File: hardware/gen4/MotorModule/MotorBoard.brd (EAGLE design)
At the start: 30.5 x 66.5 mm, 64 parts, among them IC1 XMEGA16A4A, M1O1 TEST_PT, M1O2 TEST_PT, M1O3 TEST_PT

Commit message: Motor board done (pending review)
layout + schematic done (got it down to 3x5 cm, couldn't go much smaller
unless I used smaller than 0806)
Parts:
- removed C14, C15, C3: 0.1uF, SparkFun-Passives:0805
- removed JP2: M20X2SHROUDED, SparkFun-Connectors:2X20_SHROUDED
- removed S1: SWITCH-MOMENTARY-2SMD-4, SparkFun-Electromechanical:TACTILE_SWITCH_TALL
- added JP3: M20X2SHROUDED_SMT, SparkFun-Connectors:2X20_SHROUDED_SMT
- added JP4: (no value), SparkFun-Connectors:1X04_SMD_RA_FEMALE
- added R16, R17: 2K, SparkFun-Resistors:0805
- added S2: TAC_SWITCHSMD, SparkFun-Retired:TACTILE-SWITCH-SMD
- added U$2: MOTORCON, gen3:GEN3CON
- moved IC2 198.0 mm to (26.2, 12.0), flipped to the bottom
- moved JP1 195.0 mm to (25.0, -4.00), turned to 180 degrees
- moved R11 182.3 mm to (21.0, 7.00)
- moved R5 182.1 mm to (28.0, 25.5), turned to 270 degrees
- moved R15 177.7 mm to (14.2, -12.0)
- moved R7 169.8 mm to (15.4, 6.24), turned to 90 degrees
- moved R9 169.3 mm to (11.5, 6.24), turned to 90 degrees
- moved C13 161.3 mm to (20.6, 8.60)
- moved C12 158.6 mm to (21.0, 11.0), turned to 180 degrees
- moved C1 155.8 mm to (21.0, 14.5), turned to 180 degrees
- moved U$1 134.2 mm to (15.0, 13.0)
- moved IC1 119.0 mm to (13.5, -4.50)
- moved GEN_4_REV_A 86.6 mm to (0.00, 55.2)
- moved FRAME7 53.5 mm to (-68.9, 53.5), flipped to the top
- moved R78 37.1 mm to (18.8, -12.5)
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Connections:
- removed net 5V: R105.2, R106.2, R107.2
- removed net N$25: C3.2, U$1.5
- removed net N$26: C14.1, U$1.4
- removed net N$27: C14.2, U$1.3
- removed net N$29: C15.1, U$1.2
- removed net N$30: C15.2, U$1.1
- net 12V: now also JP3.1, JP3.2, JP3.3, JP3.4; no longer JP2.1, JP2.2, JP2.3, JP2.4, JP2.5, JP2.6
- net 12VGND: now also JP3.37, JP3.38, JP3.39, JP3.40, R5.2; no longer JP2.35, JP2.36, JP2.37, JP2.38, JP2.39, JP2.40
- net 3.3V: now also C12.2, JP4.1, R105.2, R106.2, R107.2, R17.2, U$1.24, U$2.1, U$5.1
- net GND: now also JP4.3, R16.1, S2.4, U$1.P$1, U$2.5; no longer S1.B2, U$1.41-1, U$1.41-10, U$1.41-11, U$1.41-12, U$1.41-13, U$1.41-14, U$1.41-15, U$1.41-16, U$1.41-2, U$1.41-3, U$1.41-4, U$1.41-5, U$1.41-6, U$1.41-7, U$1.41-8, U$1.41-9
- net M1H1: now also U$1.5, U$2.3; no longer JP2.19
- net M1H2: now also U$1.3, U$2.4; no longer JP2.17
- net M1H3: now also U$1.1, U$2.2; no longer JP2.21
- net M1O1: now also U$2.10, U$2.11; no longer JP2.7, JP2.8
- net M1O2: now also U$2.8, U$2.9; no longer JP2.10, JP2.9
- net M1O3: now also U$2.6, U$2.7; no longer JP2.11, JP2.12
- net M1QA: now also JP4.2; no longer JP2.23
- net M1QB: now also JP4.4; no longer JP2.25
- net N$2: now also U$1.29; no longer U$1.30
- net N$22: now also R16.2, R17.1, U$1.2, U$1.4; no longer C3.1
- net N$3: now also JP3.31; no longer JP2.29
- net N$33: now also JP3.34, JP3.36; no longer JP2.32, JP2.34
- net N$34: now also JP3.35; no longer JP2.33
- net N$4: now also JP3.33; no longer JP2.31
- net N$45: now also JP3.29; no longer JP2.27
- net N$5: no longer R5.2
- net N$9: now also U$1.30; no longer U$1.29
- net RESET: now also S2.2; no longer S1.A2
- net VREG: no longer C12.2, U$1.24, U$5.1
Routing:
- net GND: track 0.00 -> 181.2 mm, vias 0 -> 9
- net 3.3V: track 0.00 -> 117.8 mm, vias 0 -> 8
- net 12V: track 0.00 -> 113.7 mm, vias 0 -> 5
- net 12VGND: track 0.00 -> 81.4 mm, vias 0 -> 3
- net TSENSE1: track 0.00 -> 61.8 mm, vias 0 -> 1
- net M1O1: track 0.00 -> 57.2 mm, vias 0 -> 2
- net M1O3: track 0.00 -> 54.0 mm, vias 0 -> 1
- net N$17: track 0.00 -> 49.1 mm, vias 0 -> 2
- net N$98: track 0.00 -> 46.9 mm
- net M1H1: track 0.00 -> 45.7 mm, vias 0 -> 3
- net RESET: track 0.00 -> 42.9 mm, vias 0 -> 3
- net M1O2: track 0.00 -> 40.2 mm, vias 0 -> 3
- net N$21: track 0.00 -> 39.1 mm, vias 0 -> 2
- net BREN: track 0.00 -> 37.9 mm, vias 0 -> 2
- net N$18: track 0.00 -> 37.8 mm
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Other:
- board size 30.5 x 66.5 mm -> 30.2 x 58.8 mm
- board text removed: "Pin1"

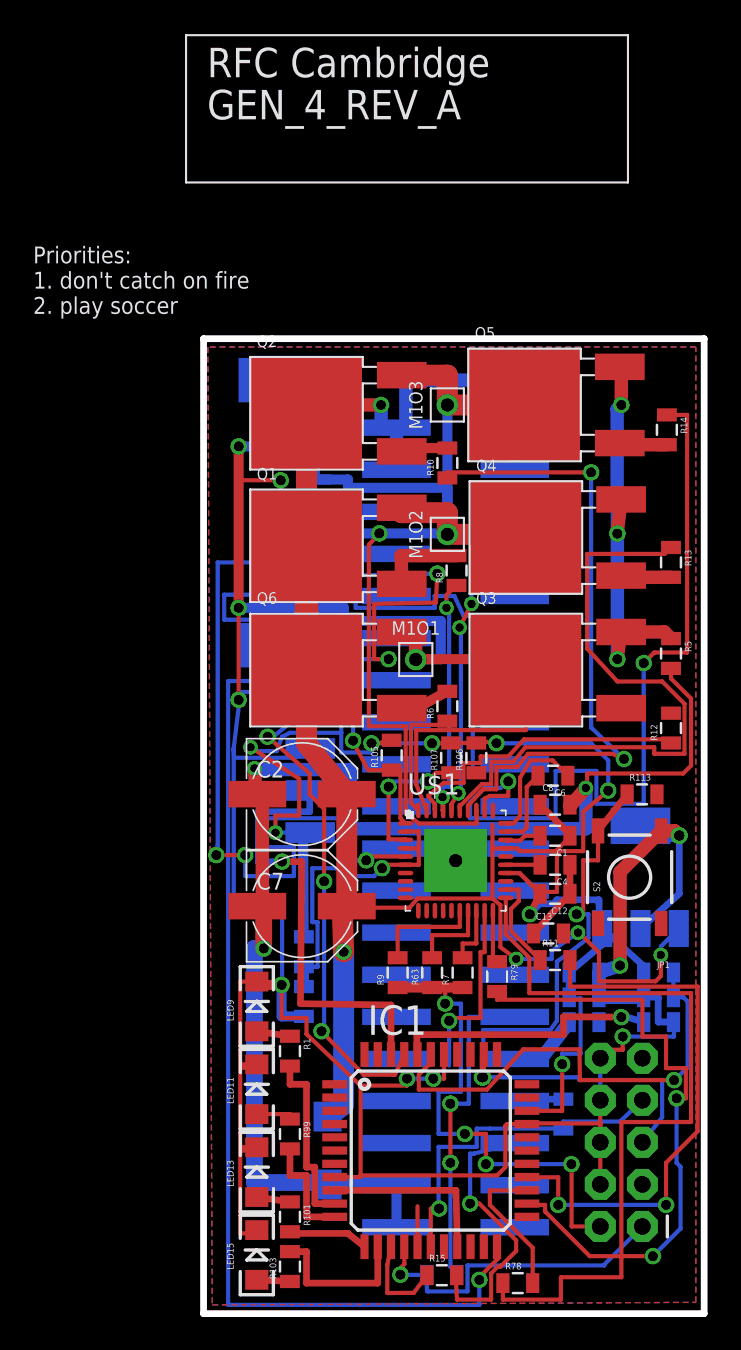
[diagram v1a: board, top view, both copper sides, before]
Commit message: Few overlap edits
Also need to fix qfn package part,  the part needs a smt pad added.
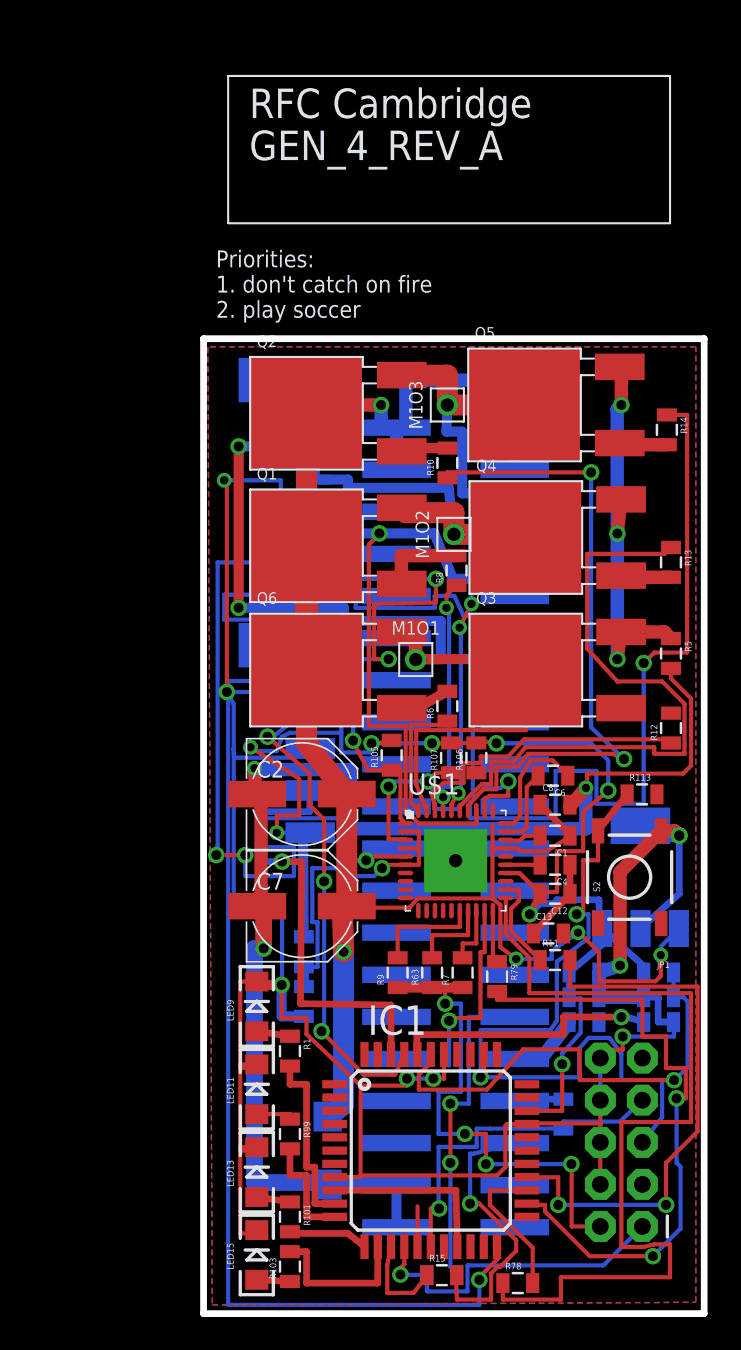
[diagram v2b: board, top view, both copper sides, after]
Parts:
- moved GEN_4_REV_A 3.54 mm to (2.54, 52.7)
- moved M1O2 0.40 mm to (14.9, 32.7)
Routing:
- net M1O3: track 54.0 -> 72.4 mm
- net M1H2: track 32.7 -> 46.4 mm
- net N$98: track 46.9 -> 53.0 mm
- net RESET: track 42.9 -> 45.9 mm, vias 3 -> 2
- net GND: track 181.2 -> 182.6 mm
- net 3.3V: track 117.8 -> 116.9 mm

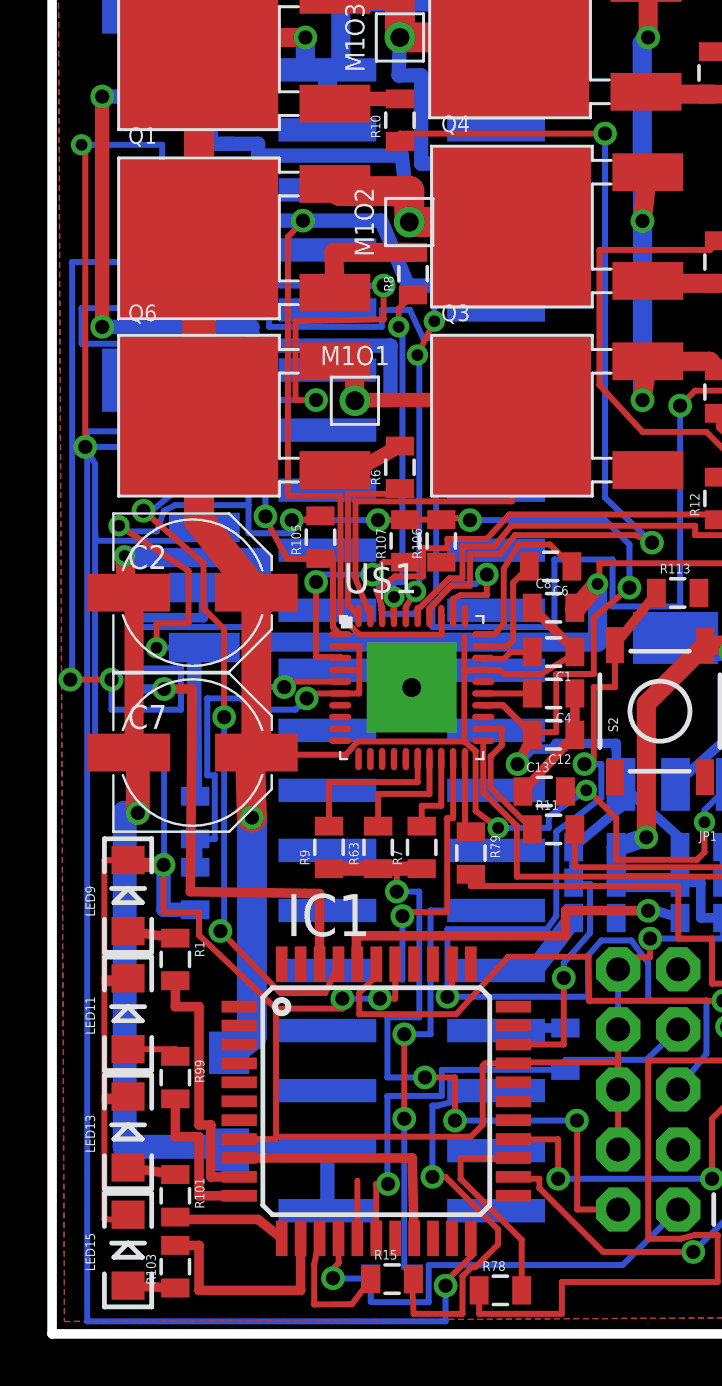
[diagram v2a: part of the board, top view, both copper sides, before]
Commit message: Slight fixes
fixed qfn package and overlap
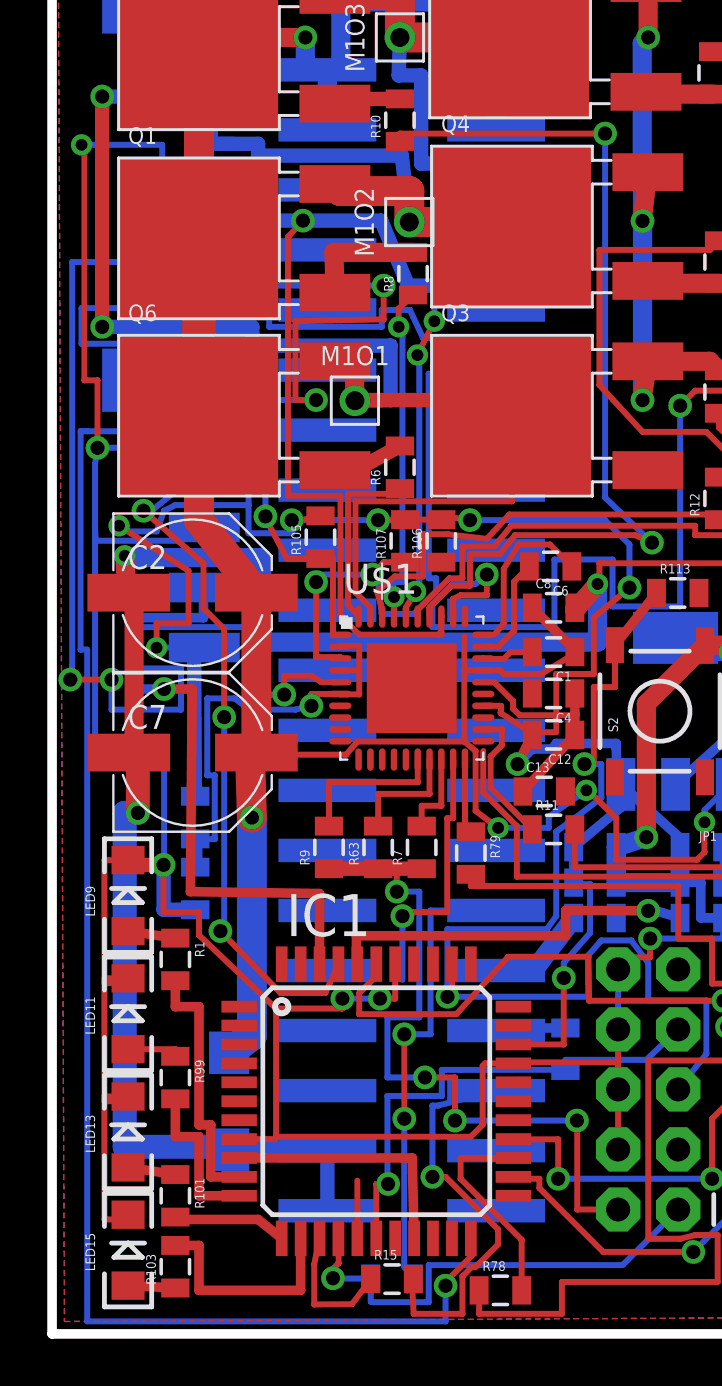
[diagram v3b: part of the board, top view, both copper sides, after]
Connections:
- net GND: now also U$1.P$3; no longer U$1.P$1
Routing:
- net GND: track 182.6 -> 187.2 mm
- net 3.3V: track 116.9 -> 114.5 mm
- net N$15: track 2.08 -> 0.00 mm
- net M1H1: track 45.8 -> 47.0 mm
- net M1H2: track 46.4 -> 47.1 mm
- net TSENSE1: track 61.8 -> 62.4 mm

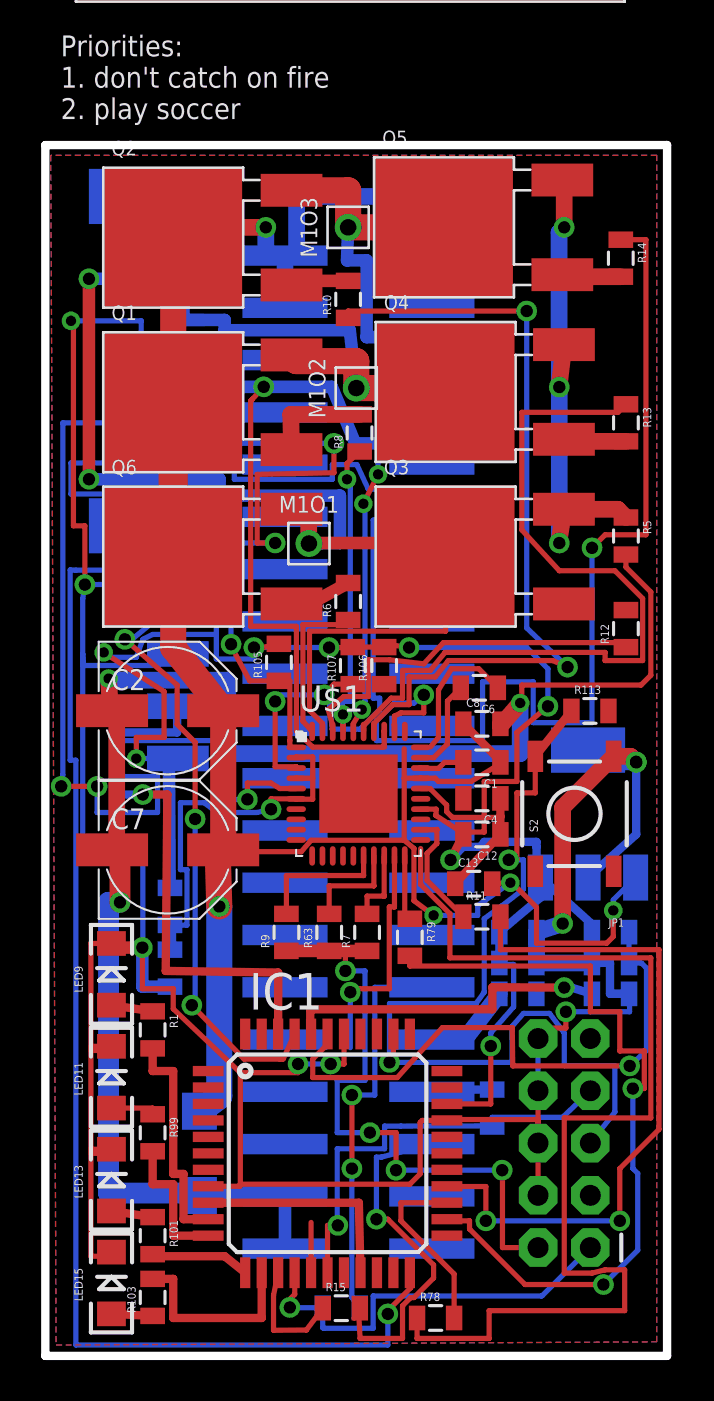
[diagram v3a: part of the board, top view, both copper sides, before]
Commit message: fixed overlaps, nearly finished routing
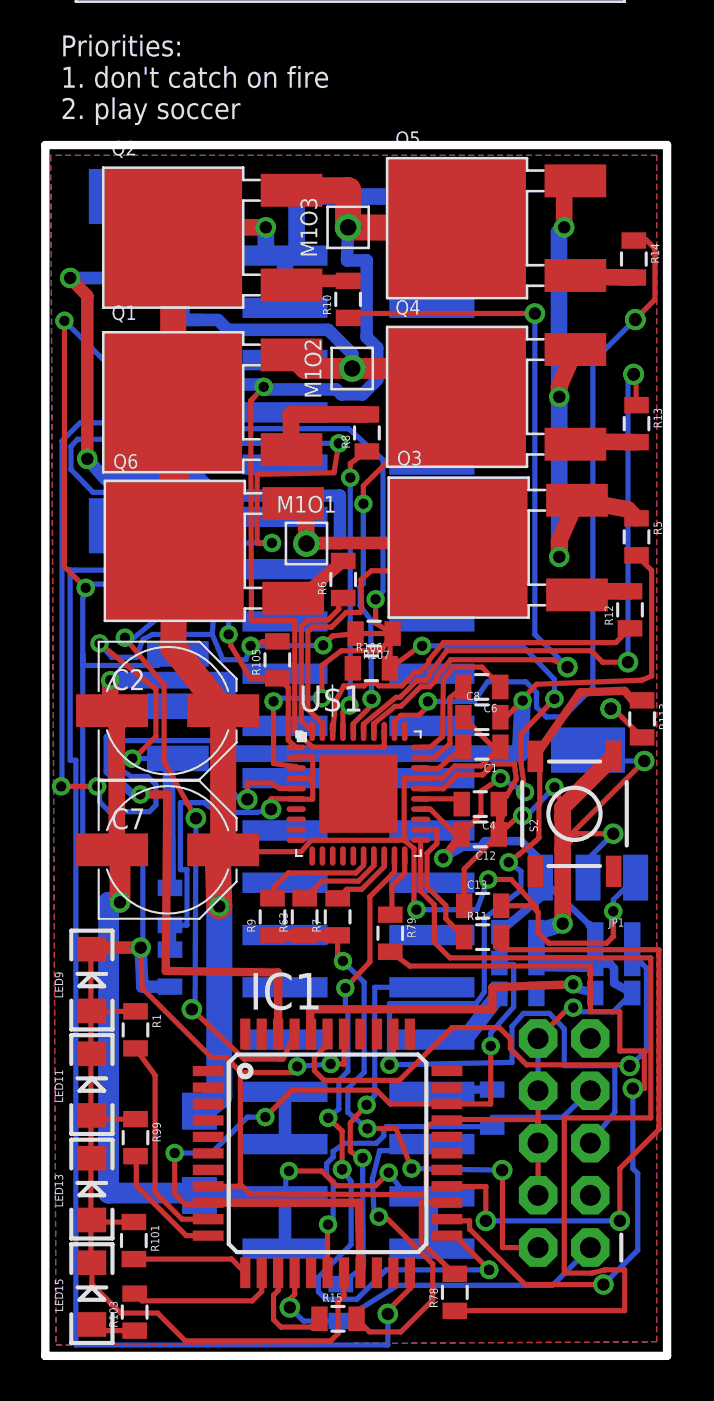
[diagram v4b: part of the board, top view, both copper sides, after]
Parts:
- moved R113 2.57 mm to (28.8, 16.6), turned to 270 degrees
- moved R107 1.87 mm to (15.8, 20.8), turned to 180 degrees
- moved R7 1.62 mm to (14.0, 6.99)
- moved R78 1.56 mm to (19.7, -11.3), turned to 90 degrees
- moved R63 1.41 mm to (12.4, 6.99)
- moved C13 1.16 mm to (21.0, 7.53)
- moved R103 1.13 mm to (4.13, -12.2)
- moved R6 1.10 mm to (14.3, 23.4)
- moved LED15 1.08 mm to (2.05, -11.3)
- moved LED13 1.05 mm to (2.05, -6.24)
- moved LED11 1.02 mm to (2.05, -1.16)
- moved R9 1.01 mm to (10.8, 6.99)
- moved R11 0.99 mm to (21.0, 6.01)
- moved LED9 0.99 mm to (2.05, 3.92)
- moved R79 0.97 mm to (16.5, 6.20)
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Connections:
- net M1O2 renamed M101
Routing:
- net PWM1: track 11.3 -> 35.6 mm, vias 1 -> 4
- net 3.3V: track 114.5 -> 136.0 mm, vias 8 -> 12
- net GND: track 187.2 -> 207.7 mm, vias 9 -> 11
- net M1O3: track 72.4 -> 54.4 mm
- net M1H2: track 47.1 -> 32.3 mm, vias 2 -> 3
- net 12VGND: track 81.3 -> 94.2 mm, vias 3 -> 5
- net N$17: track 49.4 -> 37.0 mm
- net N$18: track 38.0 -> 31.0 mm, vias 0 -> 2
- net M1O1: track 57.4 -> 61.7 mm
- net N$98: track 52.6 -> 48.8 mm
- net N$11: track 0.00 -> 3.65 mm
- net DIR: track 8.90 -> 5.39 mm
- net RESET: track 45.9 -> 49.4 mm
- net N$34: track 19.0 -> 15.9 mm
- net 12V: track 113.6 -> 110.9 mm
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
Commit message: cleaned things up a bit, extended board
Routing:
- net N$98: track 48.8 -> 41.5 mm
- net TSENSE1: track 62.4 -> 56.6 mm
- net M1QA: track 26.1 -> 22.1 mm
- net GND: track 207.7 -> 204.3 mm
- net 12VGND: track 94.2 -> 90.9 mm
- net ENABLE: track 32.4 -> 30.4 mm
- net BREN: track 38.5 -> 37.5 mm
- net VREG: track 29.7 -> 28.6 mm
- net N$8: track 16.4 -> 15.6 mm
- net RESET: track 49.4 -> 48.7 mm
- net 3.3V: track 136.0 -> 135.4 mm
- net N$22: track 19.2 -> 18.6 mm
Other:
- board size 30.2 x 58.8 mm -> 32.6 x 58.8 mm

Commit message: near finished
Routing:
- net VREG: track 28.6 -> 72.9 mm, vias 5 -> 6
- net GND: track 204.3 -> 206.8 mm
- net N$98: track 41.5 -> 42.6 mm
- net ENABLE: track 30.4 -> 31.3 mm
- net BREN: track 37.5 -> 38.3 mm

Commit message: one more airwire to route
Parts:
- moved C33 0.44 mm to (27.8, 3.29)
- moved C40 0.32 mm to (27.7, 4.71)
- moved R3 0.21 mm to (22.6, 3.33)
- moved C46 0.21 mm to (22.6, 6.17)
- moved C45 0.20 mm to (22.6, 4.75)
- moved R15 0.20 mm to (14.0, -12.3)
- moved R2 0.09 mm to (14.2, -11.7)
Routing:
- net MISO: track 0.00 -> 44.9 mm, vias 0 -> 5
- net GND: track 206.8 -> 213.9 mm, vias 11 -> 12
- net MOSI: track 17.9 -> 21.7 mm
- net SS_M: track 4.92 -> 8.57 mm
- net VREG: track 72.9 -> 75.7 mm
- net BREN: track 38.3 -> 40.5 mm
- net TSENSE1: track 56.6 -> 58.7 mm
- net ENABLE: track 31.3 -> 33.0 mm
- net N$98: track 42.6 -> 44.3 mm
- net M1H1: track 44.8 -> 43.2 mm
- net RESET: track 49.0 -> 48.1 mm
- net N$8: track 15.2 -> 16.0 mm
- net AVCC: track 26.7 -> 27.4 mm
- net 12V: track 110.9 -> 111.4 mm
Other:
- board size 32.6 x 58.8 mm -> 32.7 x 59.8 mm
